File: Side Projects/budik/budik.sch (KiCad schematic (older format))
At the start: 59 parts, among them J1 Conn_01x02_Male, J2 USB_OTG, J3 FTDI, Q1 BSS138, SW1 SW_DPST_x2, SW2 SW_DPST_x2, U1 ESP-12, U2 MCP23018-E_SP, U3 uA7805, U4 LD1117S33CTR

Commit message: Some perhaps final changes in scheme, add parts
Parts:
- added C1: 10u, Capacitors_Tantalum_SMD:CP_Tantalum_Case-B_EIA-3528-21_Hand, symbol C
- added C10, C11, C12, C13, C15, C16, C19, C2, C3, C4, C5, C7: 100n, Capacitors_Tantalum_SMD:CP_Tantalum_Case-A_EIA-3216-18_Hand, symbol C
- C14: renamed from C4; footprint Capacitors_Tantalum_SMD:CP_Tantalum_Case-B_EIA-3528-21_Hand -> Capacitors_SMD:CP_Elec_5x5.3
- C18: renamed from C6; footprint Capacitors_Tantalum_SMD:CP_Tantalum_Case-B_EIA-3528-21_Hand -> Capacitors_SMD:CP_Elec_5x5.3
- R2: value 10k -> 300R
- R5, R6: value 1k -> 150R
- SW1, SW2: footprint 7_segment:button_12mm -> Buttons_Switches_THT:SW_PUSH_6mm_h5mm
- renumbered C5 to C17, C1 to C6, C2 to C8, C3 to C9
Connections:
- net +5V: now also LED1.1 (VCC), LED11.1 (VCC), LED3.1 (VCC), LED5.1 (VCC), LED7.1 (VCC), LED9.1 (VCC); no longer LED1.3 (GND), LED11.3 (GND), LED3.3 (GND), LED5.3 (GND), LED7.3 (GND), LED9.3 (GND)
- net DATA_LED_5V: now also LED1.4 (DIN); no longer LED1.2 (DOUT)
- net GND: now also C1.2, C10.2, C11.2, C12.2, C13.2, C15.2, C16.2, C19.2, C2.2, C3.2, C4.2, C5.2, C7.2; no longer LED1.1 (VCC), LED10.3 (GND), LED11.1 (VCC), LED12.3 (GND), LED2.3 (GND), LED3.1 (VCC), LED4.3 (GND), LED5.1 (VCC), LED6.3 (GND), LED7.1 (VCC), LED8.3 (GND), LED9.1 (VCC), U1.9 (GND)
- net at LED3.2 (DOUT): now also LED5.4 (DIN); no longer LED1.4 (DIN)
- net at LED3.4 (DIN): now also LED1.2 (DOUT); no longer LED5.2 (DOUT)
- net at LED7.2 (DOUT): now also LED9.4 (DIN); no longer LED5.4 (DIN)
- net at LED7.4 (DIN): now also LED5.2 (DOUT); no longer LED9.2 (DOUT)
- net at LED11.2 (DOUT): now also LED12.4 (DIN); no longer LED9.4 (DIN)
- net at LED11.4 (DIN): now also LED9.2 (DOUT); no longer LED12.4 (DIN)
- new net: C1.1, U1.9 (GND)
- new net: C2.1, LED1.3 (GND)
- new net: C3.1, LED2.3 (GND)
- new net: C5.1, LED4.3 (GND)
- new net: C10.1, LED6.3 (GND)
- new net: C12.1, LED8.3 (GND)
- new net: C15.1, LED10.3 (GND)
- new net: C19.1, LED12.3 (GND)
- new net: C4.1, LED3.3 (GND)
- new net: C7.1, LED5.3 (GND)
- new net: C11.1, LED7.3 (GND)
- new net: C13.1, LED9.3 (GND)
- new net: C16.1, LED11.3 (GND)

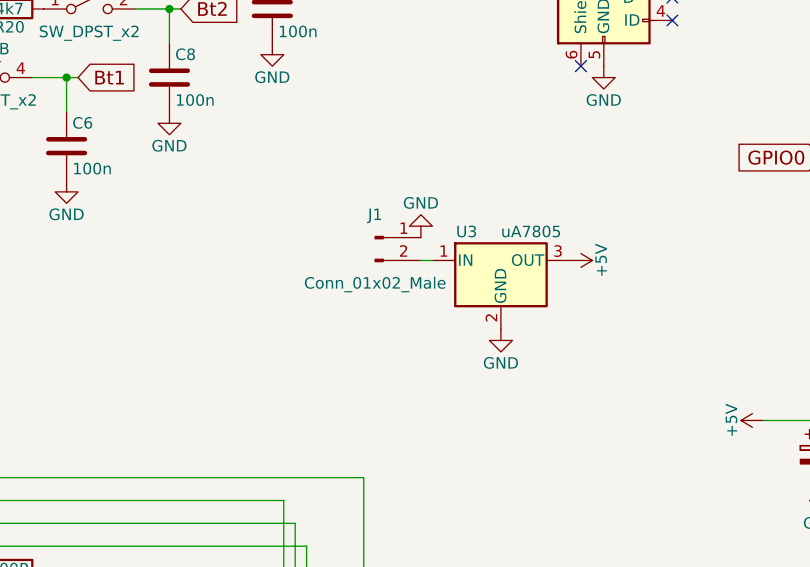
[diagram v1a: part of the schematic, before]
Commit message: Inited pcb, add led_placement.py
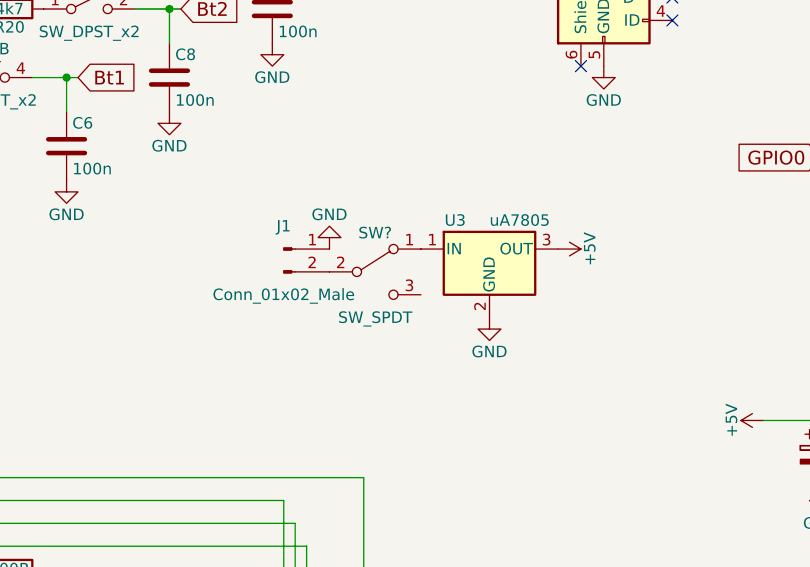
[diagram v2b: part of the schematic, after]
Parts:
- added SW?: SW_SPDT, symbol SW_SPDT
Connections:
- net at J1.2 (Pin_2): now also SW?.2 (B); no longer U3.1 (IN)
- new net: SW?.1 (A), U3.1 (IN)
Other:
- moved on the sheet: J1, U3
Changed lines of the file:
@@
 L Conn_01x02_Male J1
 U 1 1 5B004D3F
-P 6950 4550
-F 0 "J1" H 6950 4650 50  0000 C CNN
-F 1 "Conn_01x02_Male" H 6950 4350 50  0000 C CNN
-F 2 "Pin_Headers:Pin_Header_Angled_1x02_Pitch2.54mm" H 6950 4550 50  0001 C CNN
-F 3 "" H 6950 4550 50  0001 C CNN
-	1    6950 4550
+P 6550 4600
+F 0 "J1" H 6550 4700 50  0000 C CNN
+F 1 "Conn_01x02_Male" H 6550 4400 50  0000 C CNN
+F 2 "Pin_Headers:Pin_Header_Angled_1x02_Pitch2.54mm" H 6550 4600 50  0001 C CNN
+F 3 "" H 6550 4600 50  0001 C CNN
+	1    6550 4600
 	1    0    0    -1
 $EndComp
@@
 L GND #PWR37
 U 1 1 5B005929
-P 7150 4550
-F 0 "#PWR37" H 7150 4300 50  0001 C CNN
-F 1 "GND" H 7150 4400 50  0000 C CNN
-F 2 "" H 7150 4550 50  0001 C CNN
-F 3 "" H 7150 4550 50  0001 C CNN
-	1    7150 4550
+P 6750 4600
+F 0 "#PWR37" H 6750 4350 50  0001 C CNN
+F 1 "GND" H 6750 4450 50  0000 C CNN
+F 2 "" H 6750 4600 50  0001 C CNN
+F 3 "" H 6750 4600 50  0001 C CNN
+	1    6750 4600
 	-1   0    0    1
 $EndComp
@@
 L uA7805 U3
 U 1 1 5B00FCCE
-P 7500 4650
-F 0 "U3" H 7350 4775 50  0000 C CNN
-F 1 "uA7805" H 7500 4775 50  0000 L CNN
-F 2 "L7805:78XXS" H 7525 4500 50  0001 L CIN
-F 3 "" H 7500 4600 50  0001 C CNN
-	1    7500 4650
+P 7450 4600
+F 0 "U3" H 7300 4725 50  0000 C CNN
+F 1 "uA7805" H 7450 4725 50  0000 L CNN
+F 2 "L7805:78XXS" H 7475 4450 50  0001 L CIN
+F 3 "" H 7450 4550 50  0001 C CNN
+	1    7450 4600
 	1    0    0    -1
 $EndComp
@@
 L +5V #PWR39
 U 1 1 5B011BFA
-P 7800 4650
-F 0 "#PWR39" H 7800 4500 50  0001 C CNN
-F 1 "+5V" H 7800 4790 50  0000 C CNN
-F 2 "" H 7800 4650 50  0001 C CNN
-F 3 "" H 7800 4650 50  0001 C CNN
-	1    7800 4650
+P 7750 4600
+F 0 "#PWR39" H 7750 4450 50  0001 C CNN
+F 1 "+5V" H 7750 4740 50  0000 C CNN
+F 2 "" H 7750 4600 50  0001 C CNN
+F 3 "" H 7750 4600 50  0001 C CNN
+	1    7750 4600
 	0    1    1    0
 $EndComp
@@
 L GND #PWR38
 U 1 1 5B011C62
-P 7500 4950
-F 0 "#PWR38" H 7500 4700 50  0001 C CNN
-F 1 "GND" H 7500 4800 50  0000 C CNN
-F 2 "" H 7500 4950 50  0001 C CNN
-F 3 "" H 7500 4950 50  0001 C CNN
-	1    7500 4950
+P 7450 4900
+F 0 "#PWR38" H 7450 4650 50  0001 C CNN
+F 1 "GND" H 7450 4750 50  0000 C CNN
+F 2 "" H 7450 4900 50  0001 C CNN
+F 3 "" H 7450 4900 50  0001 C CNN
+	1    7450 4900
 	1    0    0    -1
 $EndComp
@@
 	0    1    1    0
 $EndComp
-Wire Wire Line
-	7200 4650 7150 4650
 $Comp
 L C C1
@@
 	-1   0    0    1
 $EndComp
+$Comp
+L SW_SPDT SW?
+U 1 1 5B09D87D
+P 6950 4700
+F 0 "SW?" H 6950 4870 50  0000 C CNN
+F 1 "SW_SPDT" H 6950 4500 50  0000 C CNN
+F 2 "" H 6950 4700 50  0001 C CNN
+F 3 "" H 6950 4700 50  0001 C CNN
+	1    6950 4700
+	1    0    0    -1
+$EndComp
 $EndSCHEMATC

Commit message: Add some pcb parts
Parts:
- SW3: renamed from SW?; footprint (none) -> 7_segment:switch
- renumbered C2 to C1, C5 to C11, C3 to C12, C1 to C13, C6 to C14, C8 to C15, C9 to C16, C14 to C17, C17 to C18, C18 to C19, C4 to C2, C7 to C3, C11 to C4, C13 to C5, C16 to C6, C19 to C7, C15 to C8, C12 to C9, LED6 to LED10, LED4 to LED11, LED2 to LED12, LED3 to LED2, LED5 to LED3, LED7 to LED4, LED9 to LED5, LED11 to LED6, LED12 to LED7, LED10 to LED8, LED8 to LED9, R9 to R10, R10 to R11, R11 to R12, R12 to R13, R13 to R14, R14 to R15, R15 to R16, R16 to R17, R17 to R18, R18 to R19, R1 to R2, R19 to R20, R20 to R21, R21 to R22, R22 to R23, R23 to R24, R24 to R25, R25 to R26, R26 to R27, R27 to R28, R2 to R3, R3 to R4, R4 to R5, R5 to R6, R6 to R7, R7 to R8, R8 to R9
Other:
- moved on the sheet: C1, C10, C11, C12, C2, C3, C4, C5, C6, C7, C8, C9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

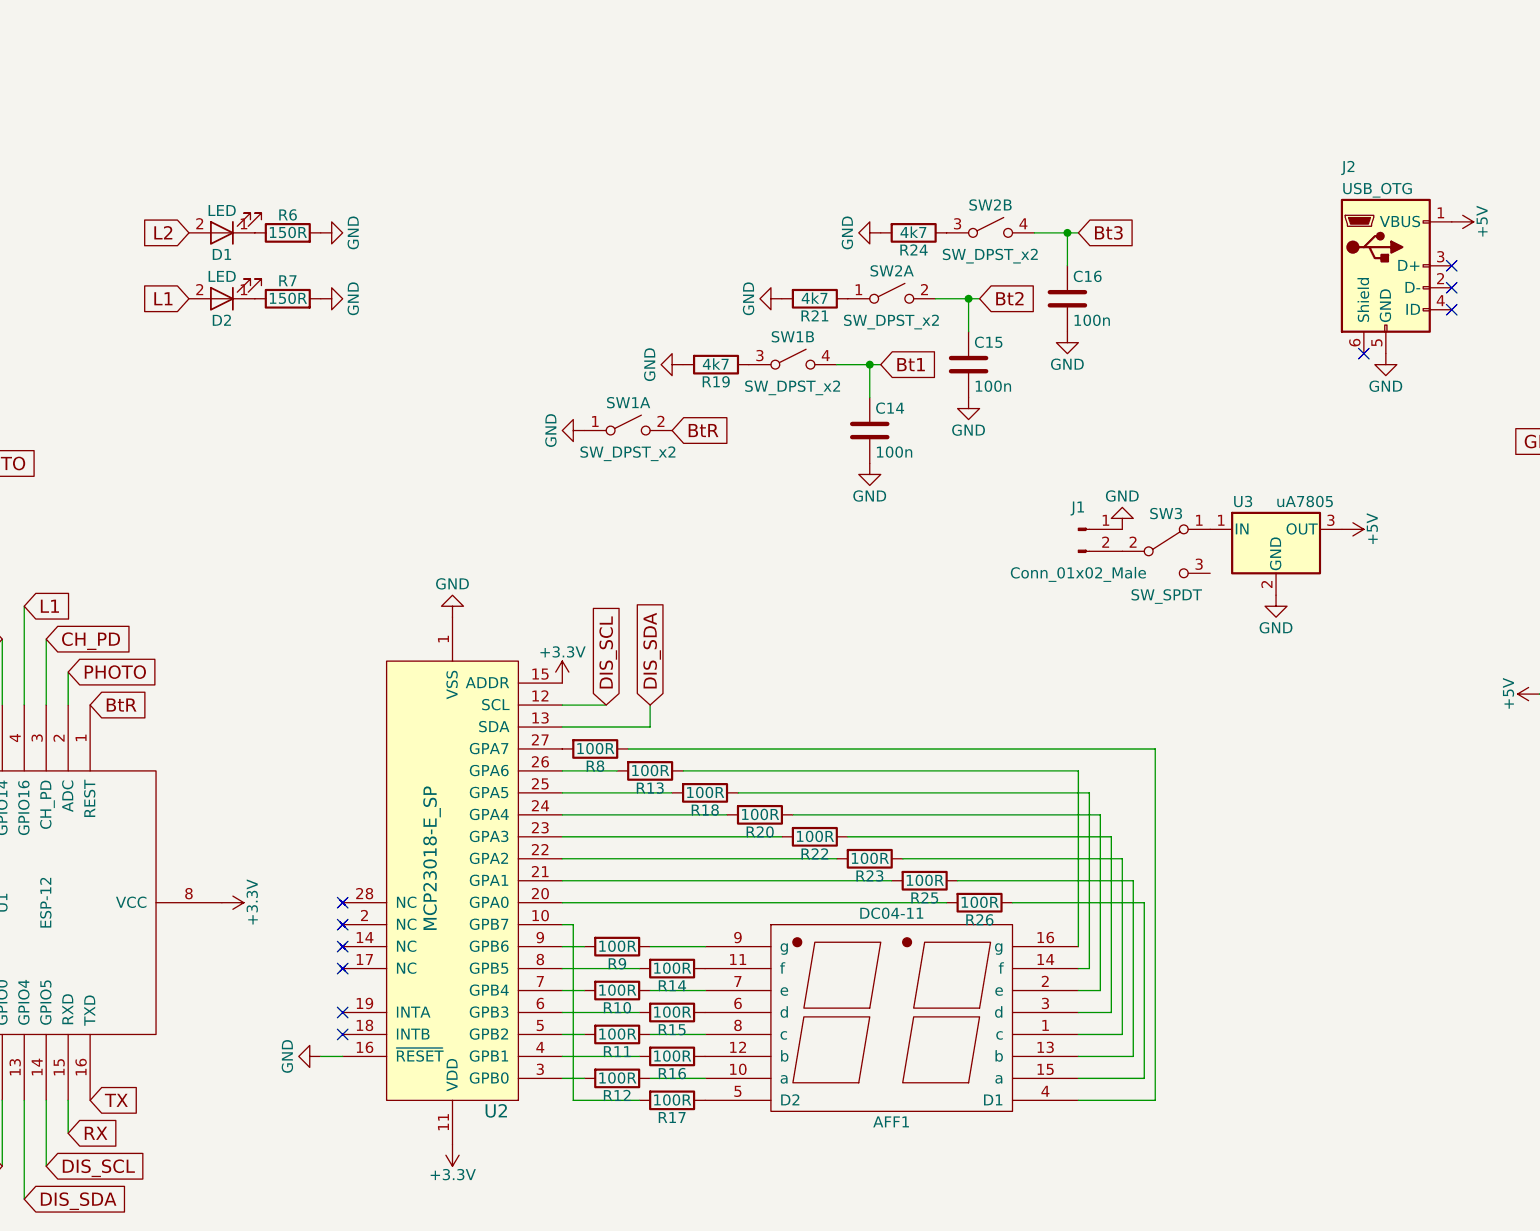
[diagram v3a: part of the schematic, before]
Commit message: Draw most of parts (only power missing).
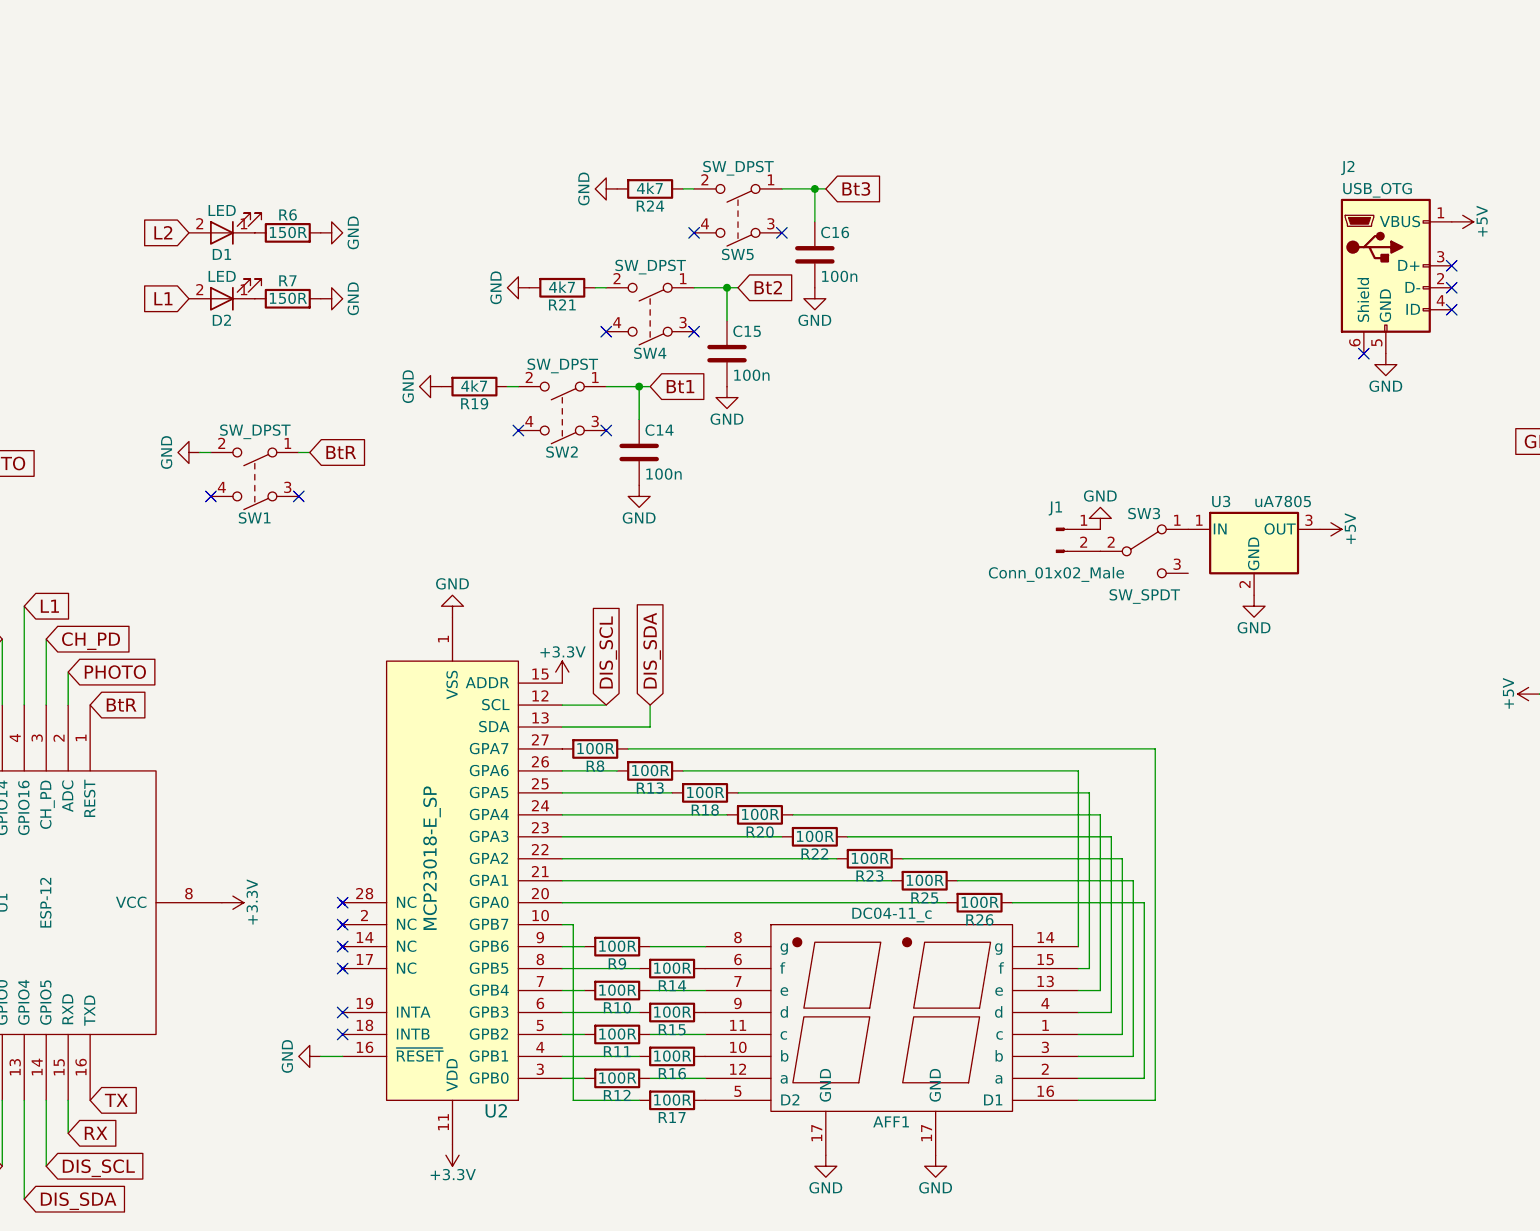
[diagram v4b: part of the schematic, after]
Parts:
- removed AFF1: DC04-11, 7_segment:7segment_double, symbol DC04-11
- removed SW1, SW2: SW_DPST_x2, Buttons_Switches_THT:SW_PUSH_6mm_h5mm, symbol SW_DPST_x2-RESCUE-budik
- added AFF1: DC04-11_c, symbol DC04-11_c
- added SW1: SW_DPST, Buttons_Switches_THT:SW_PUSH_6mm, symbol SW_DPST
- added SW2, SW4, SW5: SW_DPST, Buttons_Switches_THT:SW_PUSH-12mm, symbol SW_DPST
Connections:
- net Bt1: now also SW2.1
- net Bt2: now also SW4.1
- net Bt3: now also SW5.1
- net BtR: now also SW1.1
- net GND: now also AFF1.17 (GND), SW1.2
- net at R23.1: now also AFF1.1 (c)
- net at R12.1: now also AFF1.12 (a)
- net at R14.1: now also AFF1.6 (f)
- net at R16.1: now also AFF1.10 (b)
- net at R25.1: now also AFF1.3 (b)
- net at R18.1: now also AFF1.15 (f)
- net at R26.1: now also AFF1.2 (a)
- net at R13.1: now also AFF1.14 (g)
- net at R20.1: now also AFF1.13 (e)
- net at R22.1: now also AFF1.4 (d)
- net at R8.1: now also AFF1.16 (D1)
- net at R17.1: now also AFF1.5 (D2)
- net at R15.1: now also AFF1.9 (d)
- net at R10.1: now also AFF1.7 (e)
- net at R11.1: now also AFF1.11 (c)
- net at R9.1: now also AFF1.8 (g)
- net at R24.1: now also SW5.2
- net at R19.1: now also SW2.2
- net at R21.1: now also SW4.2
- no-connect marks 13 -> 21
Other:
- moved on the sheet: C14, C15, C16, J1, R19, R21, R24, SW3, U3

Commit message: Finish PCB v_1.0.
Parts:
- added C20: 0.33u, Capacitors_SMD:C_0603_HandSoldering, symbol C
- added C21: 0.1u, Capacitors_SMD:C_0603_HandSoldering, symbol C
- C1, C10, C11, C12, C2, C3, C4, C5, C6, C7, C8, C9: footprint Capacitors_Tantalum_SMD:CP_Tantalum_Case-A_EIA-3216-18_Hand -> Capacitors_SMD:C_0603_HandSoldering
- C17: value 10uF -> 100n
- C19: value 10uF -> 10u
- U4: footprint TO_SOT_Packages_SMD:SOT-223 -> TO_SOT_Packages_SMD:ATPAK-2
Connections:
- net +5V: now also C21.2
- net GND: now also C20.1, C21.1
- net at SW3.1 (A), U3.1 (IN): now also C20.2
